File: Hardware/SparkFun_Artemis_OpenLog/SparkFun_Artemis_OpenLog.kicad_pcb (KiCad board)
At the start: 4 copper layers, 30.5 x 30.5 mm, 88 parts, among them J11 Qwiic_RA, J14 SWD, J2 Conn_01x02, J3 Conn_01x02, J4 Conn_01x06, J5 JST_2mm_LiPo, J6 microSD, J7 Conn_01x01, J8 USB_C_Receptacle, Q2 DMG2305UX, SW3 SMD_4.6x2.8mm_h2.5mm, U1 MAX810TTRG, U10 CH340E, U2 MCP73831, U3 AP2112K-3.3, U4 AP2112K-3.3, U5 BNO086, U8 Artemis Module, Y1 32.768kHz, Y3 32.768kHz

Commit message: Updates design with silk
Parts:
- added G***: LOGO, SparkFun-Aesthetic:qwiic_4mm, F.Cu at (161.5, 104.4)
- added G***: Flame, SparkFun-Aesthetic:SparkFun_Flame_3mm, B.Cu at (140.2, 104.4)
- added G***: LOGO, SparkFun-Aesthetic:SparkFun_Logo_NoFlame_9mm, B.Cu at (148.2, 91.0)
- added kibuzzard-6A9865B8: G***, kibuzzard-6A9865B8, F.Cu at (136.4, 95.8)
- added kibuzzard-6A98662E: G***, kibuzzard-6A98662E, F.Cu at (136.4, 98.7)
- added kibuzzard-6A986638: G***, kibuzzard-6A986638, F.Cu at (136.4, 101.2)
- added kibuzzard-6A98663F: G***, kibuzzard-6A98663F, F.Cu at (136.4, 103.7)
- added kibuzzard-6A986647: G***, kibuzzard-6A986647, F.Cu at (136.4, 106.3)
- added kibuzzard-6A98664C: G***, kibuzzard-6A98664C, F.Cu at (136.4, 108.8)
- added kibuzzard-6A986671: G***, kibuzzard-6A986671, F.Cu at (161.2, 96.4)
- added kibuzzard-6A9866A0: G***, kibuzzard-6A9866A0, F.Cu at (139.9, 108.8)
- added kibuzzard-6A9866A8: G***, kibuzzard-6A9866A8, F.Cu at (142.2, 106.9)
- added kibuzzard-6A9866B0: G***, kibuzzard-6A9866B0, F.Cu at (144.7, 106.6)
- added kibuzzard-6A9866B9: G***, kibuzzard-6A9866B9, F.Cu at (147.2, 111.0)
- added kibuzzard-6A9866BF: G***, kibuzzard-6A9866BF, F.Cu at (149.8, 106.6)
- added kibuzzard-6A9866C5: G***, kibuzzard-6A9866C5, F.Cu at (152.3, 111.0)
- added kibuzzard-6A9866CC: G***, kibuzzard-6A9866CC, F.Cu at (154.5, 106.6)
- added kibuzzard-6A986700: G***, kibuzzard-6A986700, F.Cu at (139.6, 92.9)
- added kibuzzard-6A98670C: G***, kibuzzard-6A98670C, F.Cu at (143.4, 103.4)
- added kibuzzard-6A98671E: G***, kibuzzard-6A98671E, F.Cu at (143.4, 104.7)
- added kibuzzard-6A98675F: G***, kibuzzard-6A98675F, B.Cu at (153.6, 90.7)
- added kibuzzard-6A986773: G***, kibuzzard-6A986773, B.Cu at (158.3, 90.7)
- added kibuzzard-6A986792: G***, kibuzzard-6A986792, B.Cu at (158.0, 93.3)
- added kibuzzard-6A9867BB: G***, kibuzzard-6A9867BB, B.Cu at (159.3, 94.5)
- added kibuzzard-6A9867E8: G***, kibuzzard-6A9867E8, B.Cu at (162.8, 113.9)
- added kibuzzard-6A9867EE: G***, kibuzzard-6A9867EE, B.Cu at (162.2, 115.2)
- added kibuzzard-6A9867F7: G***, kibuzzard-6A9867F7, B.Cu at (160.2, 113.3)
- added kibuzzard-6A986804: G***, kibuzzard-6A986804, B.Cu at (159.3, 115.2)
- added kibuzzard-6A98681E: G***, kibuzzard-6A98681E, B.Cu at (139.9, 108.8)
- added kibuzzard-6A986832: G***, kibuzzard-6A986832, B.Cu at (136.4, 111.4)
- added kibuzzard-6A98683A: G***, kibuzzard-6A98683A, B.Cu at (136.4, 108.8)
- added kibuzzard-6A986851: G***, kibuzzard-6A986851, B.Cu at (136.4, 106.3)
- added kibuzzard-6A98685A: G***, kibuzzard-6A98685A, B.Cu at (136.4, 103.7)
- added kibuzzard-6A98686C: G***, kibuzzard-6A98686C, B.Cu at (136.4, 101.2)
- added kibuzzard-6A986874: G***, kibuzzard-6A986874, B.Cu at (136.4, 98.7)
- added kibuzzard-6A98687A: G***, kibuzzard-6A98687A, B.Cu at (136.4, 95.8)
- added kibuzzard-6A9868B3: G***, kibuzzard-6A9868B3, B.Cu at (139.6, 92.6)
- added kibuzzard-6A986903: G***, kibuzzard-6A986903, F.Cu at (136.1, 112.6)

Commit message: Updates the 5V symbol
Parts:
- renumbered C32 to C1, C3 to C10, C10 to C11, C1 to C12, C43 to C13, C2 to C14, C42 to C15, C44 to C16, C9 to C17, C6 to C18, C8 to C19, C33 to C2, C46 to C20, C7 to C21, C5 to C22, C31 to C3, C30 to C4, C29 to C5, C41 to C6, C40 to C7, C4 to C8, C11 to C9, D6 to D1, D3 to D2, D12 to D3, D11 to D4, D1 to D5, D2 to D6, D20 to D7, D9 to D8, FID3 to FID2, FID2 to FID3, G1 to G2, J8 to J1, J4 to J2, J14 to J3, J7 to J4, J2 to J6, J3 to J7, J11 to J8, J6 to J9, JP0 to JP1, Q2 to Q1, R29 to R10, R2 to R11, R28 to R12, R9 to R13, R10 to R14, R7 to R15, R6 to R16, R11 to R17, R3 to R18, R22 to R19, R8 to R2, R23 to R20, R26 to R3, R27 to R4, R25 to R5, R24 to R6, R4 to R7, R5 to R8, R12 to R9, ST3 to ST2, ST2 to ST3, SW3 to SW1, TP0 to TP2, TP4 to TP3, TP2 to TP4, TP3 to TP5, U10 to U2, U8 to U3, U2 to U4, U3 to U5, U5 to U6, U4 to U7, Y3 to Y1, Y1 to Y2
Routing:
- net (no net): track 17.0 -> 19.0 mm
- net Net-(J1-SHIELD): track 2.03 -> 0.00 mm
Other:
- board text added: "Finish: Lead-Free"
- board text removed: "Finish: ENIG"

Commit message: Updates power symbols for VBATT, 3.3V, and VCC
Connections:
- C1 pad 1: VCC_1 -> VCC
- C2 pad 1: VCC_1 -> VCC
- C3 pad 2: VCC_1 -> VCC
- R12 pad 2: VCC_1 -> VCC
- U3 pad VDD@36: VCC_1 -> VCC
- U3 pad VDD@37: VCC_1 -> VCC
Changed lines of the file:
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@@
 			(layers "F.Cu" "F.Mask" "F.Paste")
 			(roundrect_rratio 0.25)
-			(net "VCC_1")
+			(net "VCC")
 			(pintype "passive")
 		)
@@
 			(layers "F.Cu" "F.Mask" "F.Paste")
 			(roundrect_rratio 0.25)
-			(net "VCC_1")
+			(net "VCC")
 			(pintype "passive")
 		)
@@
 			(layers "F.Cu" "F.Mask" "F.Paste")
 			(roundrect_rratio 0.25)
-			(net "VCC_1")
+			(net "VCC")
 			(pintype "passive")
 		)
@@
 			(layers "F.Cu" "F.Mask" "F.Paste")
 			(roundrect_rratio 0.127)
-			(net "VCC_1")
+			(net "VCC")
 			(pinfunction "VDD*2_VDD@36")
 			(pintype "bidirectional")
@@
 			(layers "F.Cu" "F.Mask" "F.Paste")
 			(roundrect_rratio 0.127)
-			(net "VCC_1")
+			(net "VCC")
 			(pinfunction "VDD*2_VDD@37")
 			(pintype "bidirectional")
@@
 			(layers "B.Cu" "B.Mask" "B.Paste")
 			(roundrect_rratio 0.25)
-			(net "VCC_1")
+			(net "VCC")
 			(pintype "passive")
 		)

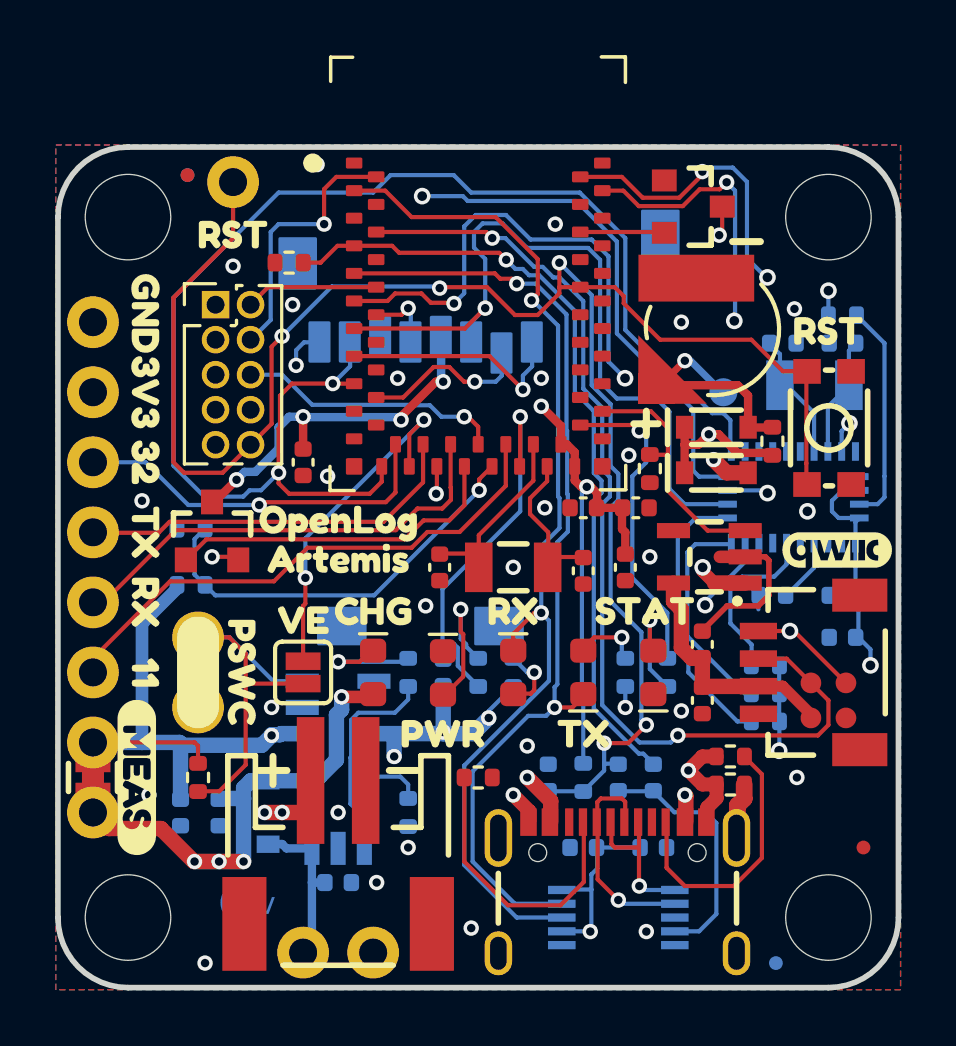
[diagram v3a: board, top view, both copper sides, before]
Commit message: Fixes the many DRC issues
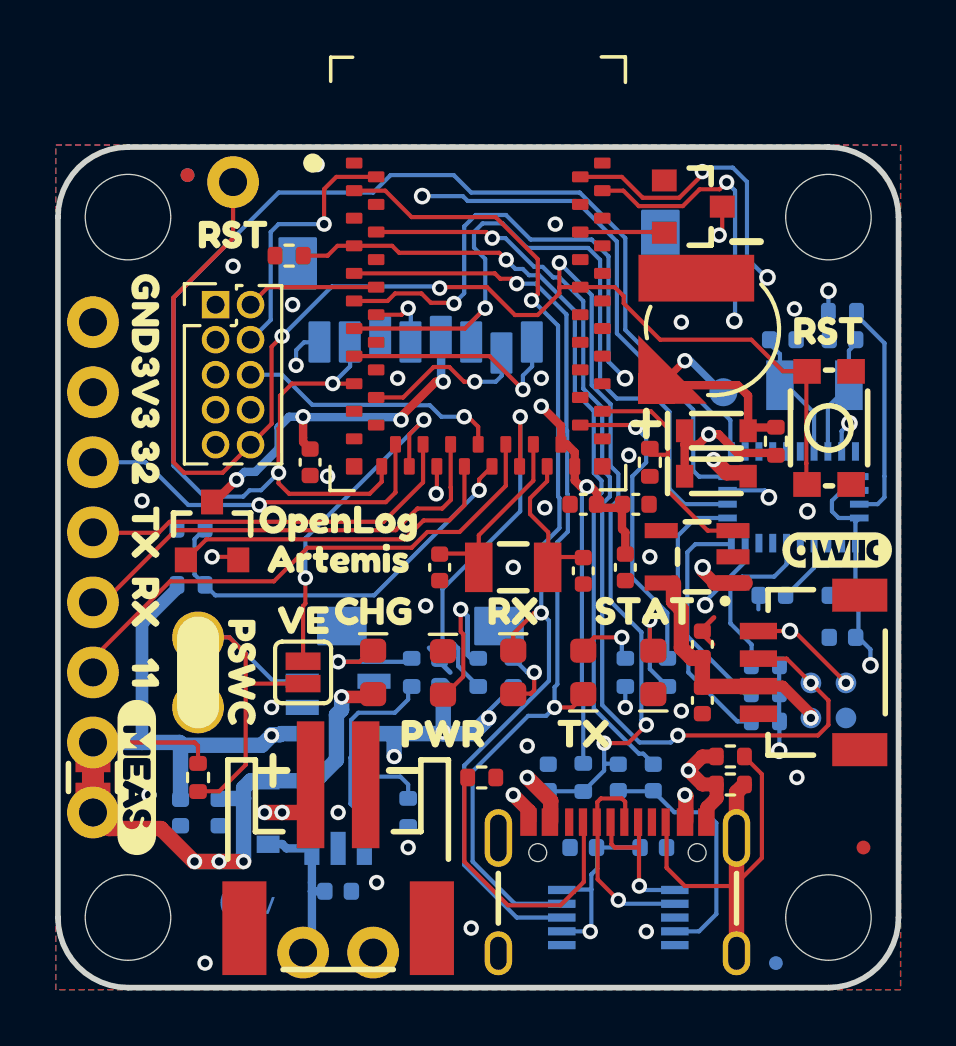
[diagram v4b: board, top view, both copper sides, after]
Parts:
- TP2, TP3, TP4, TP5: moved to B.Cu
- moved U7 0.44 mm to (156.4, 104.6)
- moved C8 0.32 mm to (143.4, 116.8)
- moved R10 0.25 mm to (141.6, 93.7)
- moved C20 0.25 mm to (142.4, 101.2)
- moved R18 0.23 mm to (154.7, 101.2)
- moved J5 0.16 mm to (143.4, 116.6)
- moved C14 0.13 mm to (147.1, 108.8)
- moved C18 0.13 mm to (159.6, 96.7)
- moved C19 0.13 mm to (161.7, 96.7)
- moved D2 0.13 mm to (157.1, 100.1)
- moved R1 0.13 mm to (159.3, 100.4)
- moved R8 0.13 mm to (146.1, 108.8)
- moved C2 0.13 mm to (154.2, 102.7)
- moved C3 0.13 mm to (152.3, 102.7)
- moved D1 0.13 mm to (157.1, 101.7)
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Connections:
- D1 pad 1: VCC_1 -> VCC
- D2 pad 1: VCC_1 -> VCC
- R1 pad 2: VCC_1 -> VCC
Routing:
- net VCC_1: track 32.7 -> 0.00 mm, vias 3 -> 0
- net VCC: track 0.00 -> 32.7 mm, vias 0 -> 3
- net (no net): track 19.0 -> 0.00 mm
- net Net-(J1-SHIELD): track 0.00 -> 10.6 mm
- net GND: track 11.8 -> 8.13 mm
- net SDA: vias 2 -> 3
- net SCL: vias 3 -> 4
- net QWIIC_3.3V: vias 0 -> 1

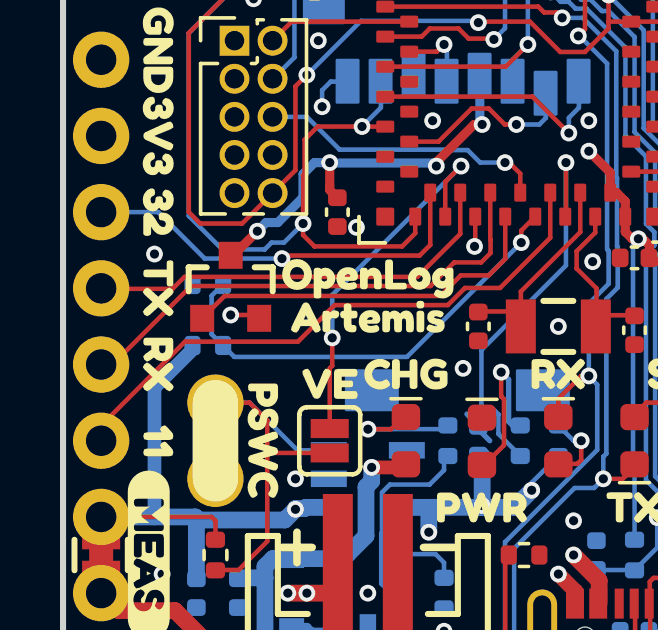
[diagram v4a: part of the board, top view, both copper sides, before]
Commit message: Updated resistor values
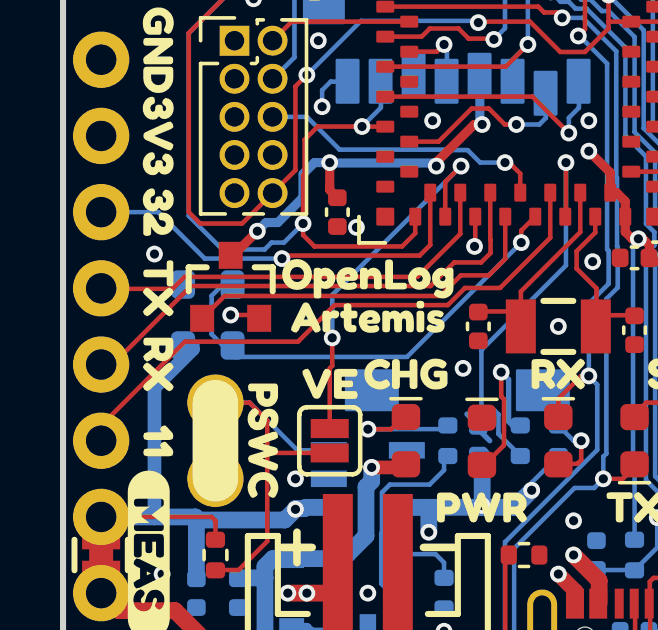
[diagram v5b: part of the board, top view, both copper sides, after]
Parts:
- JP1: value ~ -> VE
- R15: value 200k -> 2M; footprint SparkFun-Resistor:R_0402_1005Metric -> SparkFun-Resistor:R_0603_1608Metric
- R16: value 100k -> 1M; footprint SparkFun-Resistor:R_0402_1005Metric -> SparkFun-Resistor:R_0603_1608Metric
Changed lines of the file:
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@@
 			)
 		)
-		(property "Value" "~"
+		(property "Value" "VE"
 			(at 0 1.143 90)
 			(layer "F.Fab")
@@
 		)
 	)
-	(footprint "SparkFun-Resistor:R_0402_1005Metric"
+	(footprint "SparkFun-Resistor:R_0603_1608Metric"
 		(layer "B.Cu")
 		(at 138.0871 105.6386 180)
-		(descr "Resistor SMD 0402 (1005 Metric), square (rectangular) end terminal, IPC_7351 nominal, (Body size source: IPC-SM-782 page 72, https://www.pcb-3d.com/wordpress/wp-content/uploads/ipc-sm-782a_amendment_1_and_2.pdf), generated with kicad-footprint-generator")
+		(descr "Resistor SMD 0603 (1608 Metric), square (rectangular) end terminal, IPC_7351 nominal, (Body size source: IPC-SM-782 page 72, https://www.pcb-3d.com/wordpress/wp-content/uploads/ipc-sm-782a_amendment_1_and_2.pdf), generated with kicad-footprint-generator")
 		(tags "SparkFun resistor")
 		(property "Reference" "R15"
-			(at 0 1.17 0)
+			(at 0 1.43 0)
 			(layer "B.Fab")
 			(effects
@@
 			)
 		)
-		(property "Value" "200k"
-			(at 0 -1.17 0)
+		(property "Value" "2M"
+			(at 0 -1.43 0)
 			(layer "B.Fab")
 			(effects
@@
 			)
 		)
-		(property "PROD_ID" "RES-15347"
+		(property "PROD_ID" "RES-15186"
 			(at 0 0 180)
 			(unlocked yes)
@@
 		(duplicate_pad_numbers_are_jumpers no)
 		(fp_line
-			(start -0.153641 0.38)
-			(end 0.153641 0.38)
+			(start -0.237258 0.5225)
+			(end 0.237258 0.5225)
 			(stroke
 				(width 0.12)
@@
 		)
 		(fp_line
-			(start -0.153641 -0.38)
-			(end 0.153641 -0.38)
+			(start -0.237258 -0.5225)
+			(end 0.237258 -0.5225)
 			(stroke
 				(width 0.12)
@@
 		)
 		(fp_line
-			(start 0.93 0.47)
-			(end 0.93 -0.47)
+			(start 1.48 0.73)
+			(end 1.48 -0.73)
 			(stroke
 				(width 0.05)
@@
 		)
 		(fp_line
-			(start 0.93 -0.47)
-			(end -0.93 -0.47)
+			(start 1.48 -0.73)
+			(end -1.48 -0.73)
 			(stroke
 				(width 0.05)
@@
 		)
 		(fp_line
-			(start -0.93 0.47)
-			(end 0.93 0.47)
+			(start -1.48 0.73)
+			(end 1.48 0.73)
 			(stroke
 				(width 0.05)
@@
 		)
 		(fp_line
-			(start -0.93 -0.47)
-			(end -0.93 0.47)
+			(start -1.48 -0.73)
+			(end -1.48 0.73)
 			(stroke
 				(width 0.05)
@@
 		)
 		(fp_line
-			(start 0.525 0.27)
-			(end 0.525 -0.27)
+			(start 0.8 0.4125)
+			(end 0.8 -0.4125)
 			(stroke
 				(width 0.1)
@@
 		)
 		(fp_line
-			(start 0.525 -0.27)
-			(end -0.525 -0.27)
+			(start 0.8 -0.4125)
+			(end -0.8 -0.4125)
 			(stroke
 				(width 0.1)
@@
 		)
 		(fp_line
-			(start -0.525 0.27)
-			(end 0.525 0.27)
+			(start -0.8 0.4125)
+			(end 0.8 0.4125)
 			(stroke
 				(width 0.1)
@@
 		)
 		(fp_line
-			(start -0.525 -0.27)
-			(end -0.525 0.27)
+			(start -0.8 -0.4125)
+			(end -0.8 0.4125)
 			(stroke
 				(width 0.1)
@@
 		)
 		(pad "1" smd roundrect
-			(at -0.51 0 180)
-			(size 0.54 0.64)
+			(at -0.825 0 180)
+			(size 0.8 0.95)
 			(layers "B.Cu" "B.Mask" "B.Paste")
 			(roundrect_rratio 0.25)
@@
 		)
 		(pad "2" smd roundrect
-			(at 0.51 0 180)
-			(size 0.54 0.64)
+			(at 0.825 0 180)
+			(size 0.8 0.95)
 			(layers "B.Cu" "B.Mask" "B.Paste")
 			(roundrect_rratio 0.25)
@@
 		)
 		(embedded_fonts no)
-		(model "${SPARKFUN_KICAD_LIBRARY}/3dmodels/Resistor.3dshapes/R_0402_1005Metric.step"
+		(model "${SPARKFUN_KICAD_LIBRARY}/3dmodels/Resistor.3dshapes/R_0603_1608Metric.step"
 			(offset
 				(xyz 0 0 0)
@@
 		)
 	)
-	(footprint "SparkFun-Resistor:R_0402_1005Metric"
+	(footprint "SparkFun-Resistor:R_0603_1608Metric"
 		(layer "B.Cu")
 		(at 138.0871 103.6066)
-		(descr "Resistor SMD 0402 (1005 Metric), square (rectangular) end terminal, IPC_7351 nominal, (Body size source: IPC-SM-782 page 72, https://www.pcb-3d.com/wordpress/wp-content/uploads/ipc-sm-782a_amendment_1_and_2.pdf), generated with kicad-footprint-generator")
+		(descr "Resistor SMD 0603 (1608 Metric), square (rectangular) end terminal, IPC_7351 nominal, (Body size source: IPC-SM-782 page 72, https://www.pcb-3d.com/wordpress/wp-content/uploads/ipc-sm-782a_amendment_1_and_2.pdf), generated with kicad-footprint-generator")
 		(tags "SparkFun resistor")
 		(property "Reference" "R16"
-			(at 0 1.17 180)
+			(at 0 1.43 180)
 			(layer "B.Fab")
 			(effects
@@
 			)
 		)
-		(property "Value" "100k"
-			(at 0 -1.17 180)
+		(property "Value" "1M"
+			(at 0 -1.43 180)
 			(layer "B.Fab")
 			(effects
@@
 			)
 		)
-		(property "PROD_ID" "RES-25013"
+		(property "PROD_ID" "RES-07868"
 			(at 0 0 0)
 			(unlocked yes)
@@
 		(duplicate_pad_numbers_are_jumpers no)
 		(fp_line
-			(start -0.153641 -0.38)
-			(end 0.153641 -0.38)
+			(start -0.237258 -0.5225)
+			(end 0.237258 -0.5225)
 			(stroke
 				(width 0.12)
@@
 		)
 		(fp_line
-			(start -0.153641 0.38)
-			(end 0.153641 0.38)
+			(start -0.237258 0.5225)
+			(end 0.237258 0.5225)
 			(stroke
 				(width 0.12)
@@
 		)
 		(fp_line
-			(start -0.93 -0.47)
-			(end -0.93 0.47)
+			(start -1.48 -0.73)
+			(end -1.48 0.73)
 			(stroke
 				(width 0.05)
@@
 		)
 		(fp_line
-			(start -0.93 0.47)
-			(end 0.93 0.47)
+			(start -1.48 0.73)
+			(end 1.48 0.73)
 			(stroke
 				(width 0.05)
@@
 		)
 		(fp_line
-			(start 0.93 -0.47)
-			(end -0.93 -0.47)
+			(start 1.48 -0.73)
+			(end -1.48 -0.73)
 			(stroke
 				(width 0.05)
@@
 		)
 		(fp_line
-			(start 0.93 0.47)
-			(end 0.93 -0.47)
+			(start 1.48 0.73)
+			(end 1.48 -0.73)
 			(stroke
 				(width 0.05)
@@
 		)
 		(fp_line
-			(start -0.525 -0.27)
-			(end -0.525 0.27)
+			(start -0.8 -0.4125)
+			(end -0.8 0.4125)
 			(stroke
 				(width 0.1)
@@
 		)
 		(fp_line
-			(start -0.525 0.27)
-			(end 0.525 0.27)
+			(start -0.8 0.4125)
+			(end 0.8 0.4125)
 			(stroke
 				(width 0.1)
@@
 		)
 		(fp_line
-			(start 0.525 -0.27)
-			(end -0.525 -0.27)
+			(start 0.8 -0.4125)
+			(end -0.8 -0.4125)
 			(stroke
 				(width 0.1)
@@
 		)
 		(fp_line
-			(start 0.525 0.27)
-			(end 0.525 -0.27)
+			(start 0.8 0.4125)
+			(end 0.8 -0.4125)
 			(stroke
 				(width 0.1)
@@
 		)
 		(pad "1" smd roundrect
-			(at -0.51 0)
-			(size 0.54 0.64)
+			(at -0.825 0)
+			(size 0.8 0.95)
 			(layers "B.Cu" "B.Mask" "B.Paste")
 			(roundrect_rratio 0.25)
@@
 		)
 		(pad "2" smd roundrect
-			(at 0.51 0)
-			(size 0.54 0.64)
+			(at 0.825 0)
+			(size 0.8 0.95)
 			(layers "B.Cu" "B.Mask" "B.Paste")
 			(roundrect_rratio 0.25)
@@
 		)
 		(embedded_fonts no)
-		(model "${SPARKFUN_KICAD_LIBRARY}/3dmodels/Resistor.3dshapes/R_0402_1005Metric.step"
+		(model "${SPARKFUN_KICAD_LIBRARY}/3dmodels/Resistor.3dshapes/R_0603_1608Metric.step"
 			(offset
 				(xyz 0 0 0)

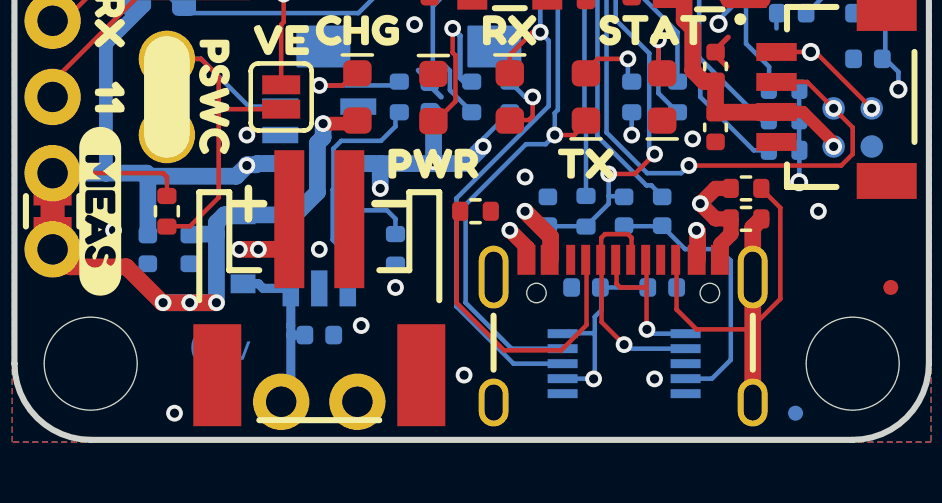
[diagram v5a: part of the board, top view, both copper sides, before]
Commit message: Fixes BNO symbol, adds parts to mosfet
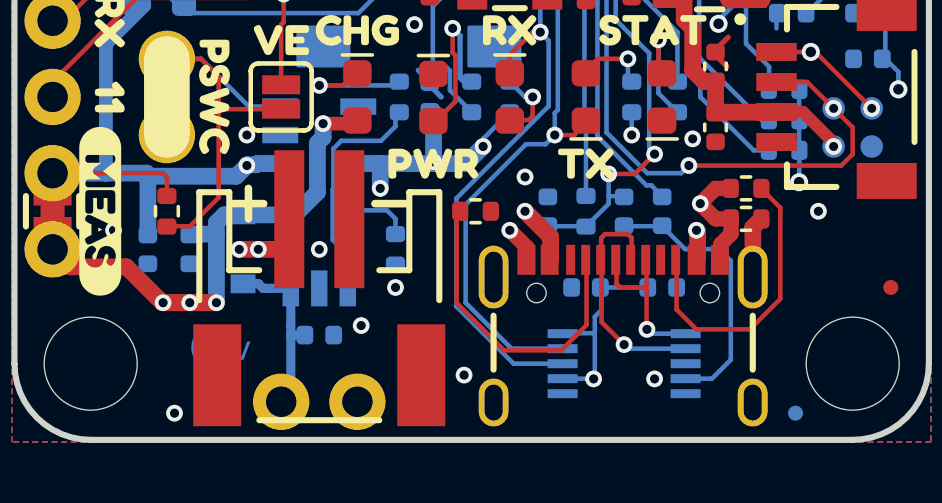
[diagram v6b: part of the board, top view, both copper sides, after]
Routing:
- net Net-(J1-SHIELD): track 10.6 -> 6.81 mm
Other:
- board text added: "v20"
- board text removed: "v10"
